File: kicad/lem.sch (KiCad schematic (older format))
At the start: 16 parts

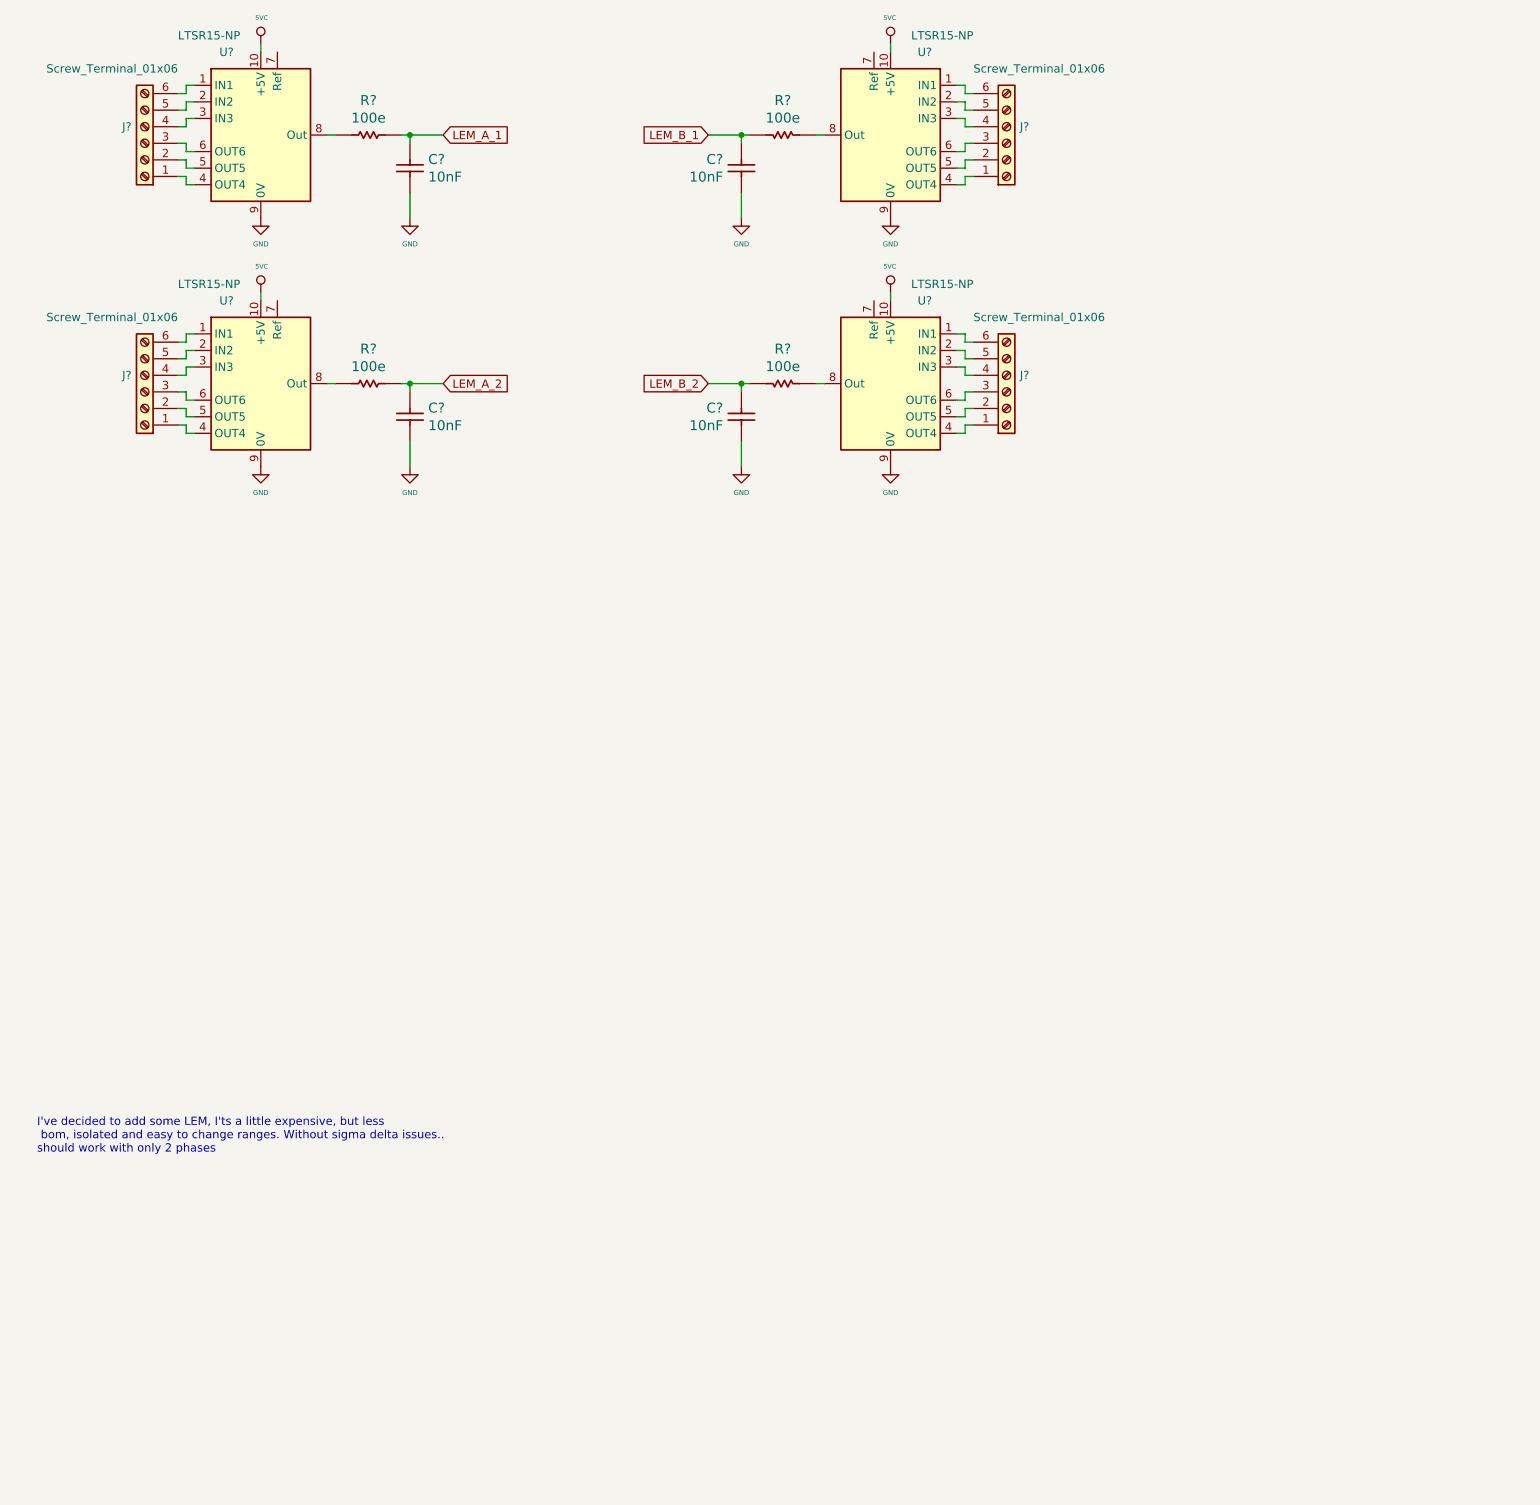
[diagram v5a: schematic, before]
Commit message: I've decided LEM lxs series, it's the best..
I've decided to use the LEM lxs, is a new series better than LTS and is
pin to pin compatible with the old one and also CAS series, so I think
it's a good option. 0.5usec rise time, multi prymari turns options, and
so..
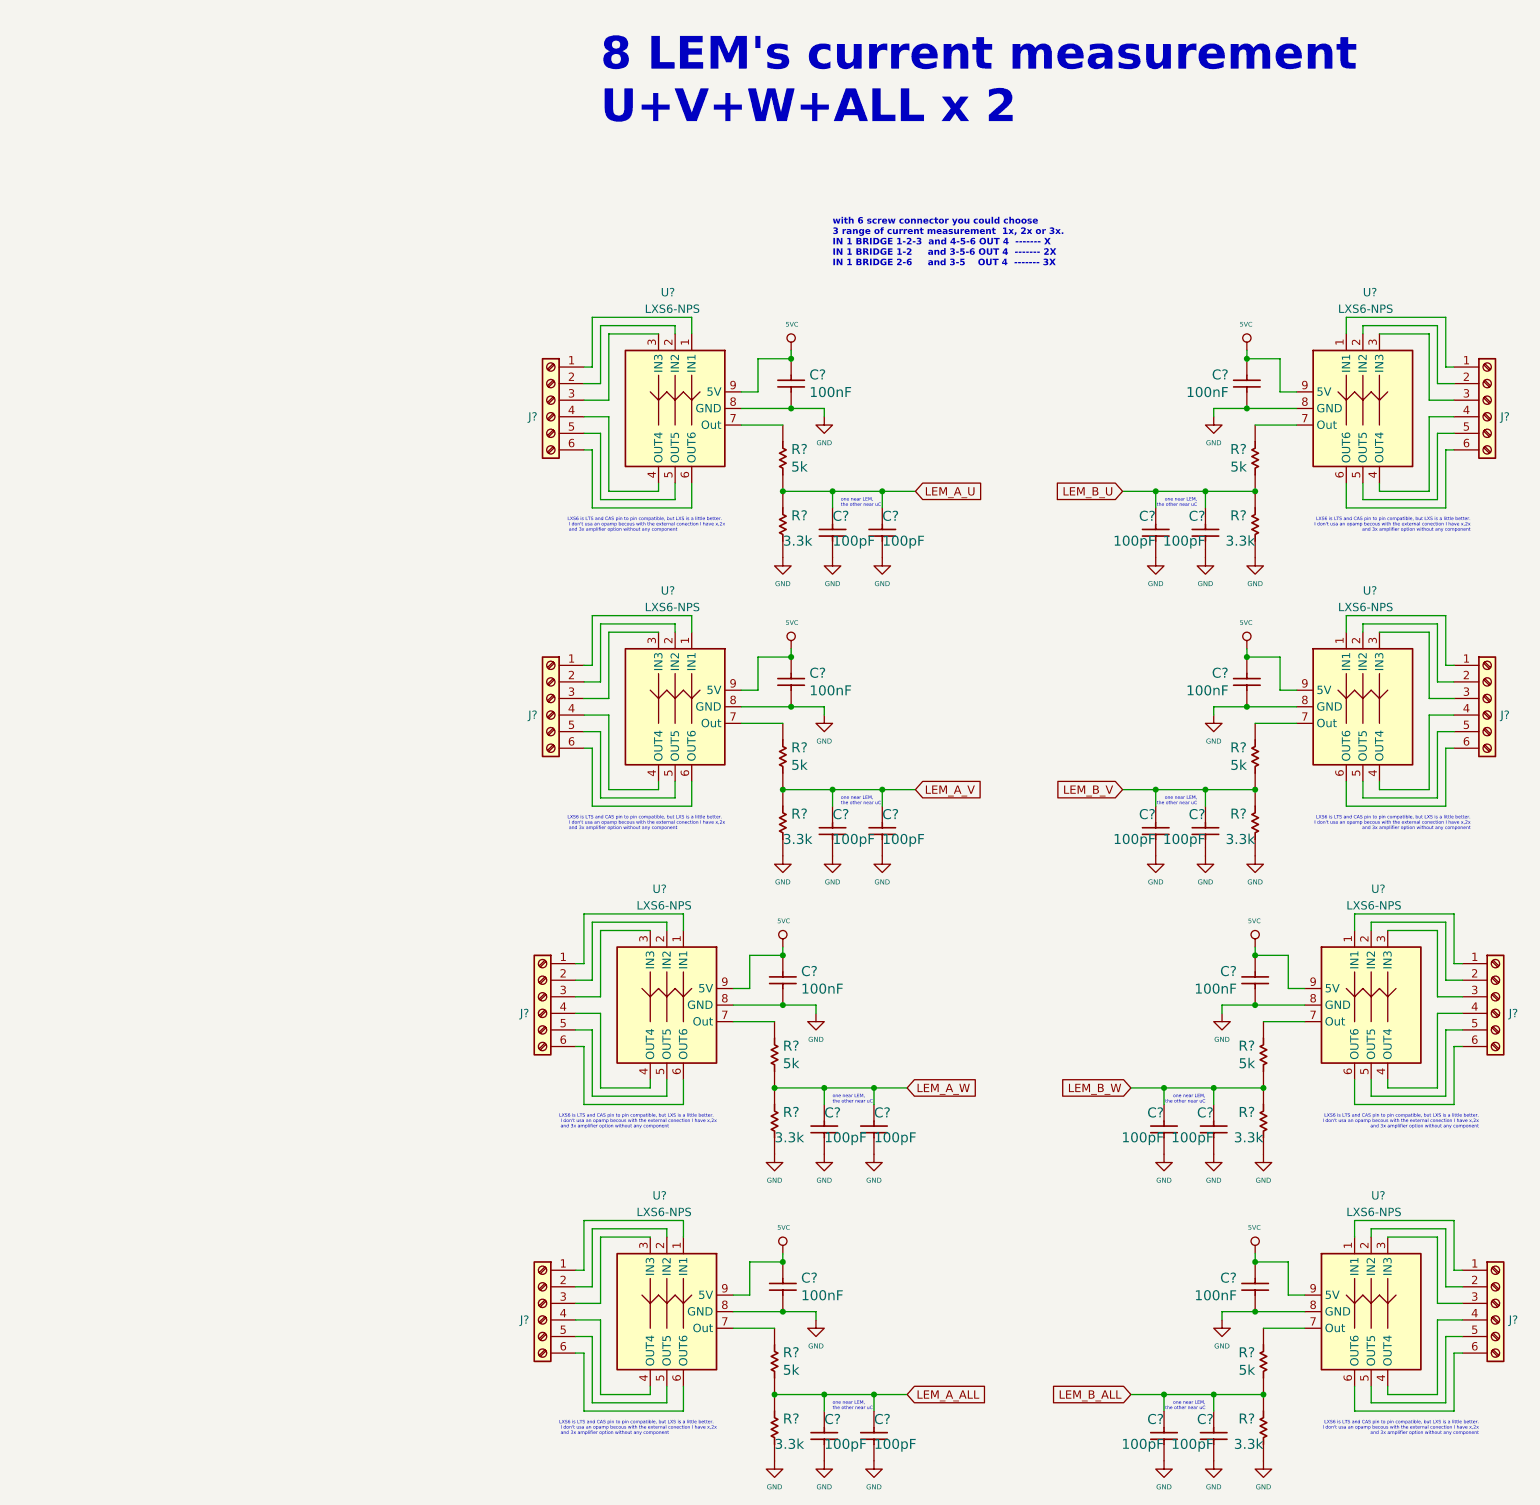
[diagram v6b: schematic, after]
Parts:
- removed C? (x3): 10nF, symbol servo:Capacitor
- removed J? (x3): Screw_Terminal_01x06, symbol Connector:Screw_Terminal_01x06
- removed R? (x4): 100e, symbol servo:Resistor
- removed U? (x4): LTSR15-NP, Sensor_Current:LEM_LTSR-NP, symbol servo:LTSR15-NP
- added C? (x8): 100nF, symbol servo:Capacitor
- added C? (x15): 100pF, symbol servo:Capacitor
- added J? (x7): Screw_Terminal_01x06, symbol Connector:Screw_Terminal_01x06
- added R? (x8): 3.3k, symbol servo:Resistor
- added R? (x8): 5k, symbol servo:Resistor
- added U? (x8): LXS6-NPS, symbol servo:LXS6-NPS
- C?: value 10nF -> 100pF
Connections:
- net 5VC: now also C?.2, C?.2, C?.2, C?.2, C?.2, C?.2, C?.2, C?.2, U?.9 (5V), U?.9 (5V), U?.9 (5V), U?.9 (5V), U?.9 (5V), U?.9 (5V), U?.9 (5V), U?.9 (5V)
- net GND: now also C?.1, C?.1, C?.1, C?.1, C?.1, C?.1, C?.1, C?.1, C?.1, C?.1, C?.1, C?.1, C?.1, C?.1, C?.1, C?.1, C?.1, C?.1, C?.1, C?.1, C?.1, C?.1, C?.1, R?.2, R?.2, R?.2, R?.2, R?.2, R?.2, R?.2, R?.2, U?.8 (GND), U?.8 (GND), U?.8 (GND), U?.8 (GND), U?.8 (GND), U?.8 (GND), U?.8 (GND), U?.8 (GND)
- net at J?.6 (Pin_6): now also U?.6 (OUT6)
- net at J?.5 (Pin_5): now also U?.5 (OUT5)
- net at J?.4 (Pin_4): now also U?.4 (OUT4)
- net at J?.1 (Pin_1): now also U?.1 (IN1)
- net at J?.2 (Pin_2): now also U?.2 (IN2)
- net at J?.3 (Pin_3): now also U?.3 (IN3)
- net LEM_A_2 renamed LEM_A_V
- net LEM_A_V: now also C?.2, R?.1, R?.2
- new net: R?.1, U?.7 (Out) (x8)
- new net: J?.1 (Pin_1), U?.1 (IN1) (x7)
- new net: J?.2 (Pin_2), U?.2 (IN2) (x7)
- new net: J?.3 (Pin_3), U?.3 (IN3) (x7)
- new net: J?.4 (Pin_4), U?.4 (OUT4) (x7)
- new net: J?.5 (Pin_5), U?.5 (OUT5) (x7)
- new net: J?.6 (Pin_6), U?.6 (OUT6) (x7)
- new net LEM_A_ALL: C?.2, C?.2, R?.1, R?.2
- new net LEM_A_U: C?.2, C?.2, R?.1, R?.2
- new net LEM_A_W: C?.2, C?.2, R?.1, R?.2
- new net LEM_B_ALL: C?.2, C?.2, R?.1, R?.2
- new net LEM_B_U: C?.2, C?.2, R?.1, R?.2
- new net LEM_B_V: C?.2, C?.2, R?.1, R?.2
- new net LEM_B_W: C?.2, C?.2, R?.1, R?.2
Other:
- note added: "8 LEM's current measurement \nU+V+W+ALL x 2"
- note added: "LXS6 is LTS and CAS pin to pin compatible, but LXS is a little better.\n I don't usa an opamp becous with the external conection I have x,2x\n and 3x amplifier option without any component"
- note added: "one near LEM, \nthe other near uC"
- note added: "with 6 screw connector you could choose\n3 range of current measurement 1x, 2x or 3x.\nIN 1 BRIDGE 1-2-3 and 4-5-6 OUT 4 ------- X\nIN 1 BRIDGE 1-2 and 3-5-6 OUT 4 ------- 2X\nIN 1 BRIDGE 2-6 and 3-5 OUT 4 ------- 3X\n"
- note removed: "I've decided to add some LEM, I'ts a little expensive, but less\n bom, isolated and easy to change ranges. Without sigma delta issues..\nshould work with only 2 phases\n"
- moved on the sheet: C?, J?
